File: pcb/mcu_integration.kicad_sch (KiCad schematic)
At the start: 28 parts, among them J1 Micro_SD_Card, U1 STM32F103RBTx, Y1 ECS-80-18-5PX-GM-TR

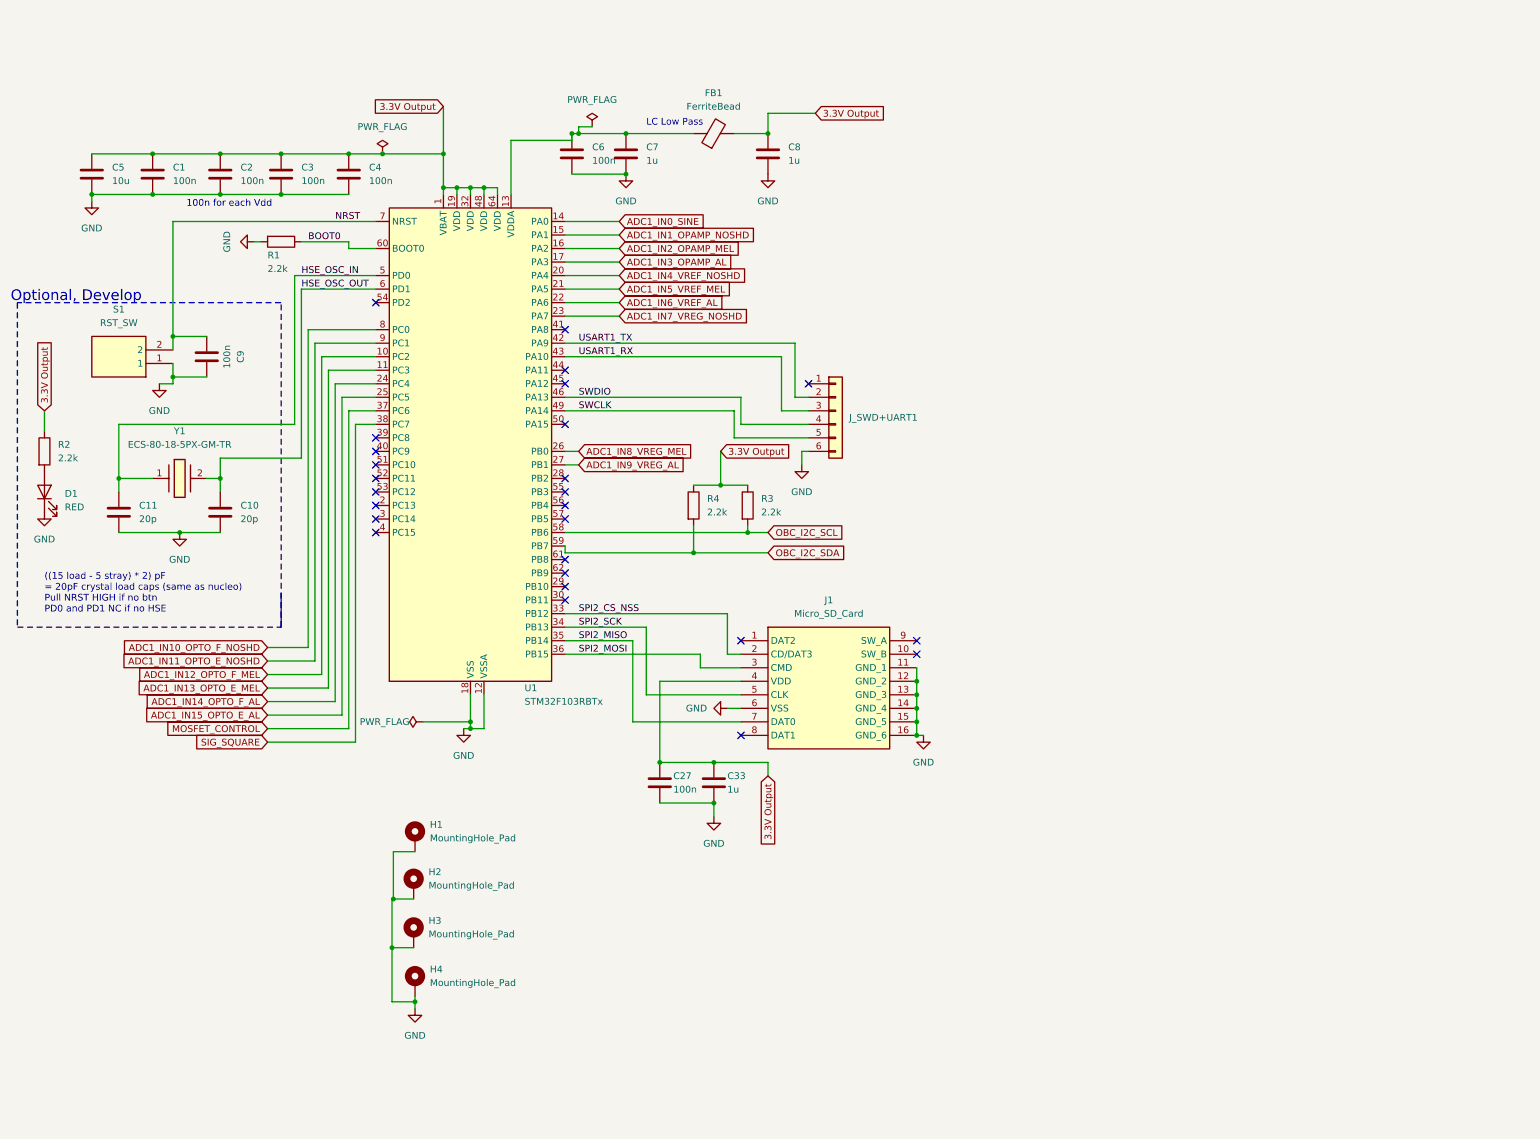
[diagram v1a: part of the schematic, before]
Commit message: SD card change
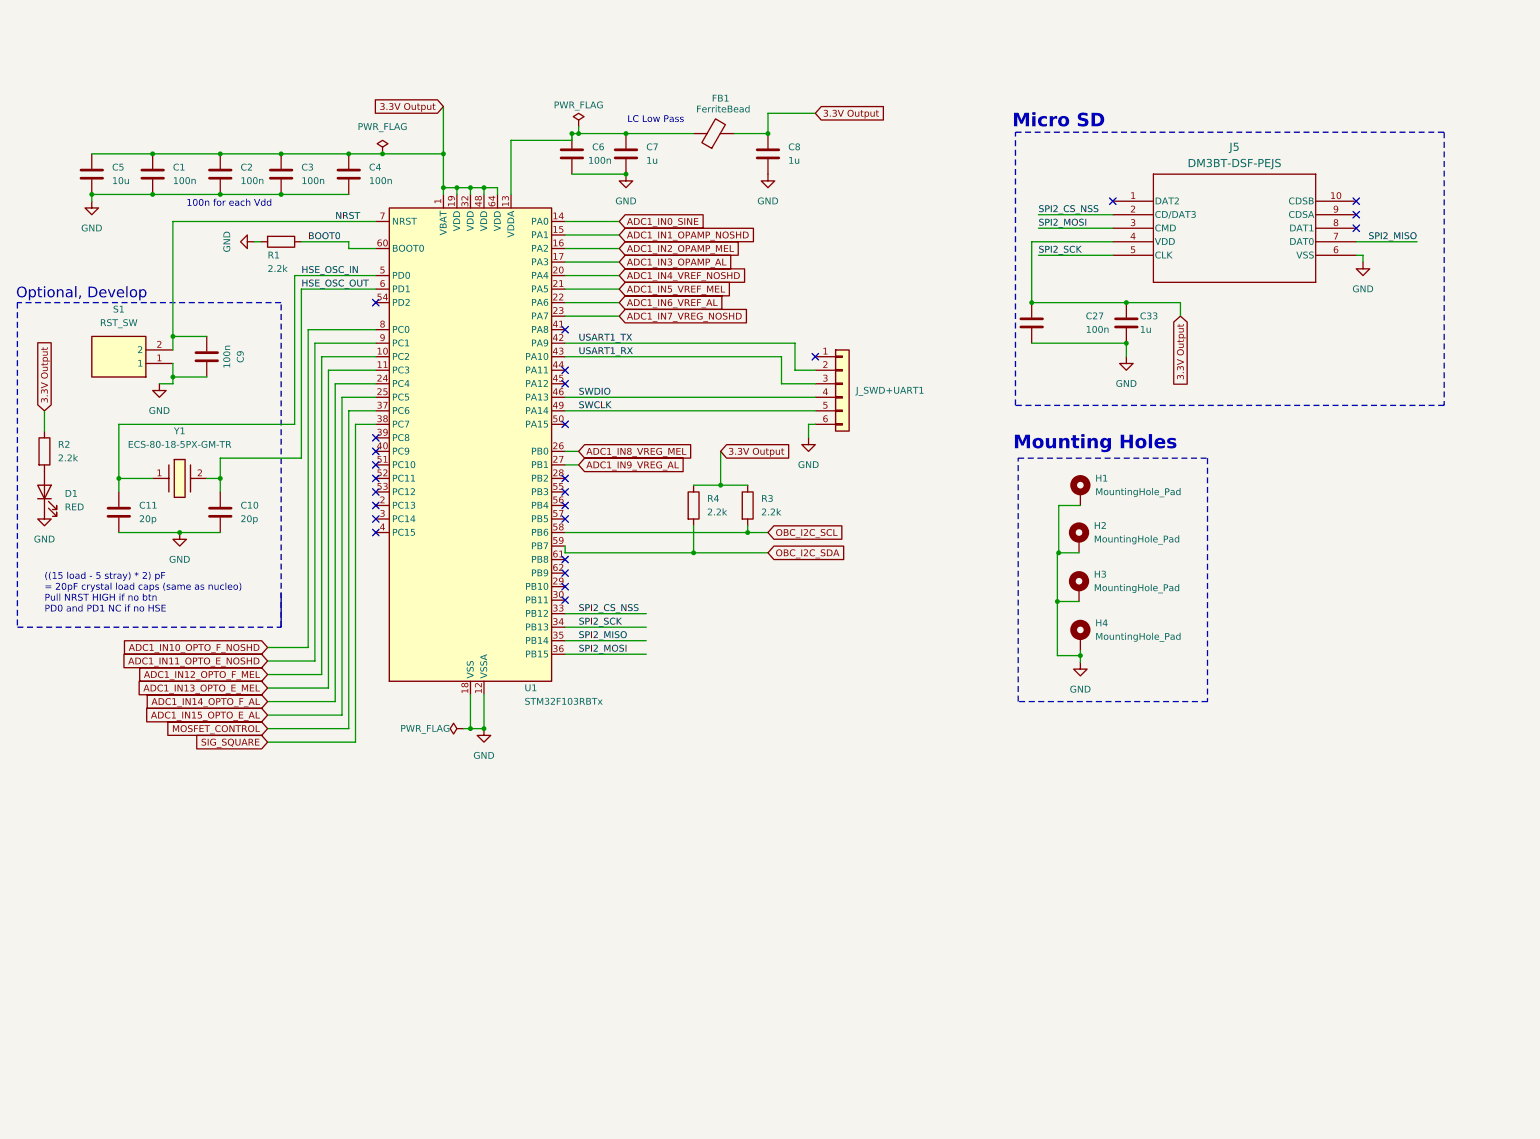
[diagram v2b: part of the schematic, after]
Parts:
- removed J1: Micro_SD_Card, capstone:22017781, symbol capstone:2201778-1
- added J5: DM3BT-DSF-PEJS, capstone:DM3BT_DSF_PEJS, symbol capstone:DM3BT-DSF-PEJS
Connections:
- net 3.3V Output: now also J5.4 (VDD)
- net GND: now also J5.6 (VSS)
- net SPI2_CS_NSS: now also J5.2 (CD/DAT3)
- net SPI2_MISO: now also J5.7 (DAT0)
- net SPI2_MOSI: now also J5.3 (CMD)
- net SPI2_SCK: now also J5.5 (CLK)
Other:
- note added: "Micro SD"
- note added: "Mounting Holes"
- moved on the sheet: C27, C33, H1, H2, H3, H4, J_SWD+UART1

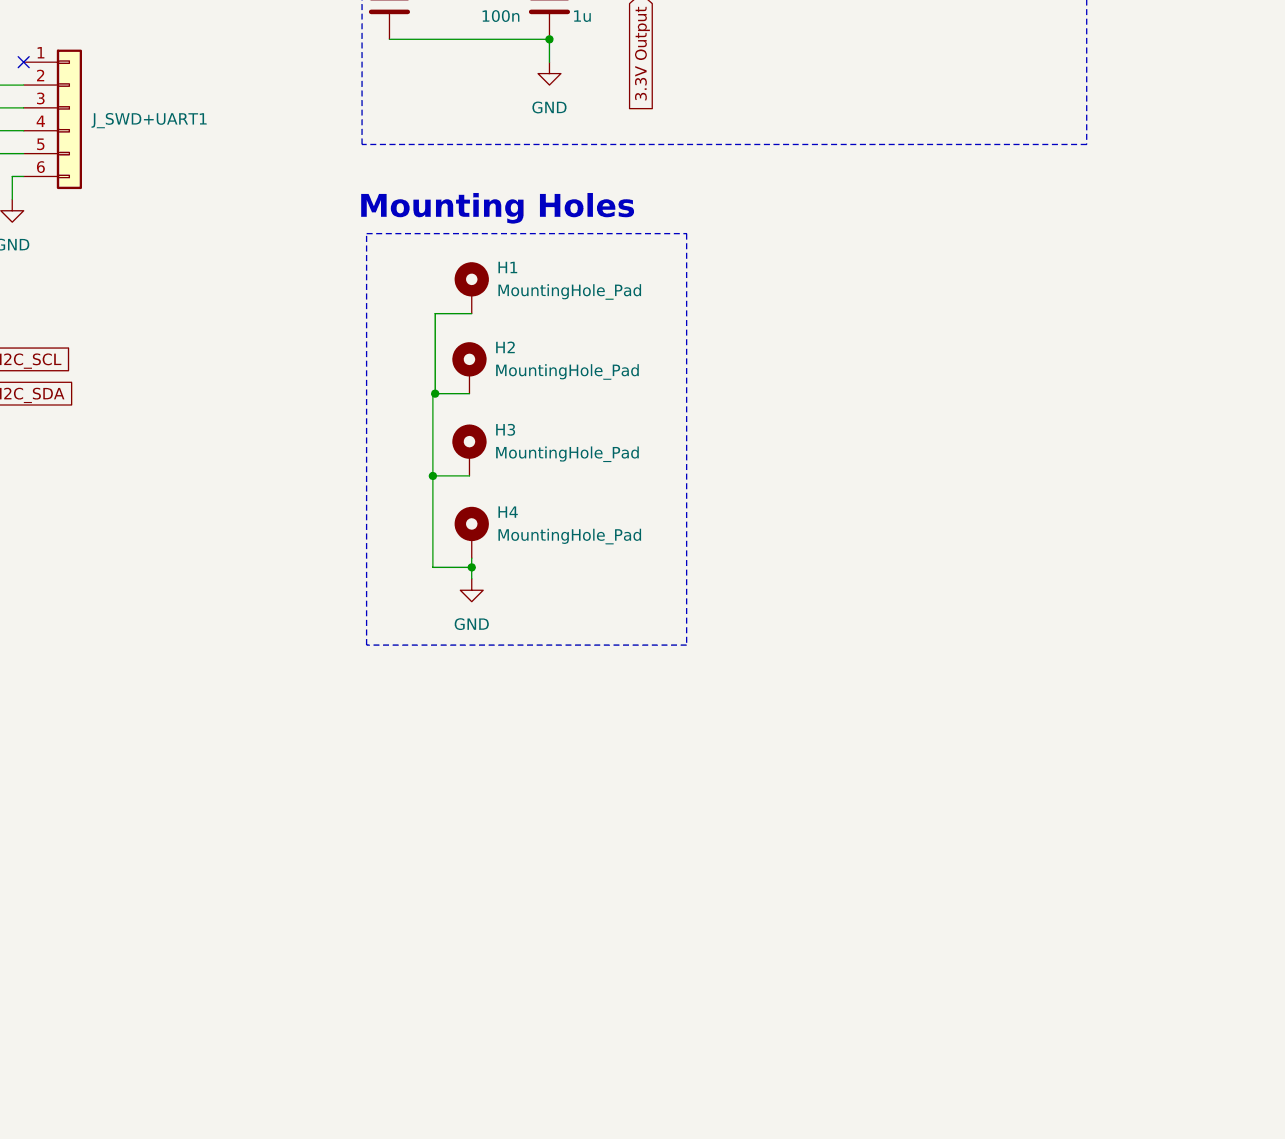
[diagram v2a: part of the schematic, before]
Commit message: Added LM35 Temp Sensor
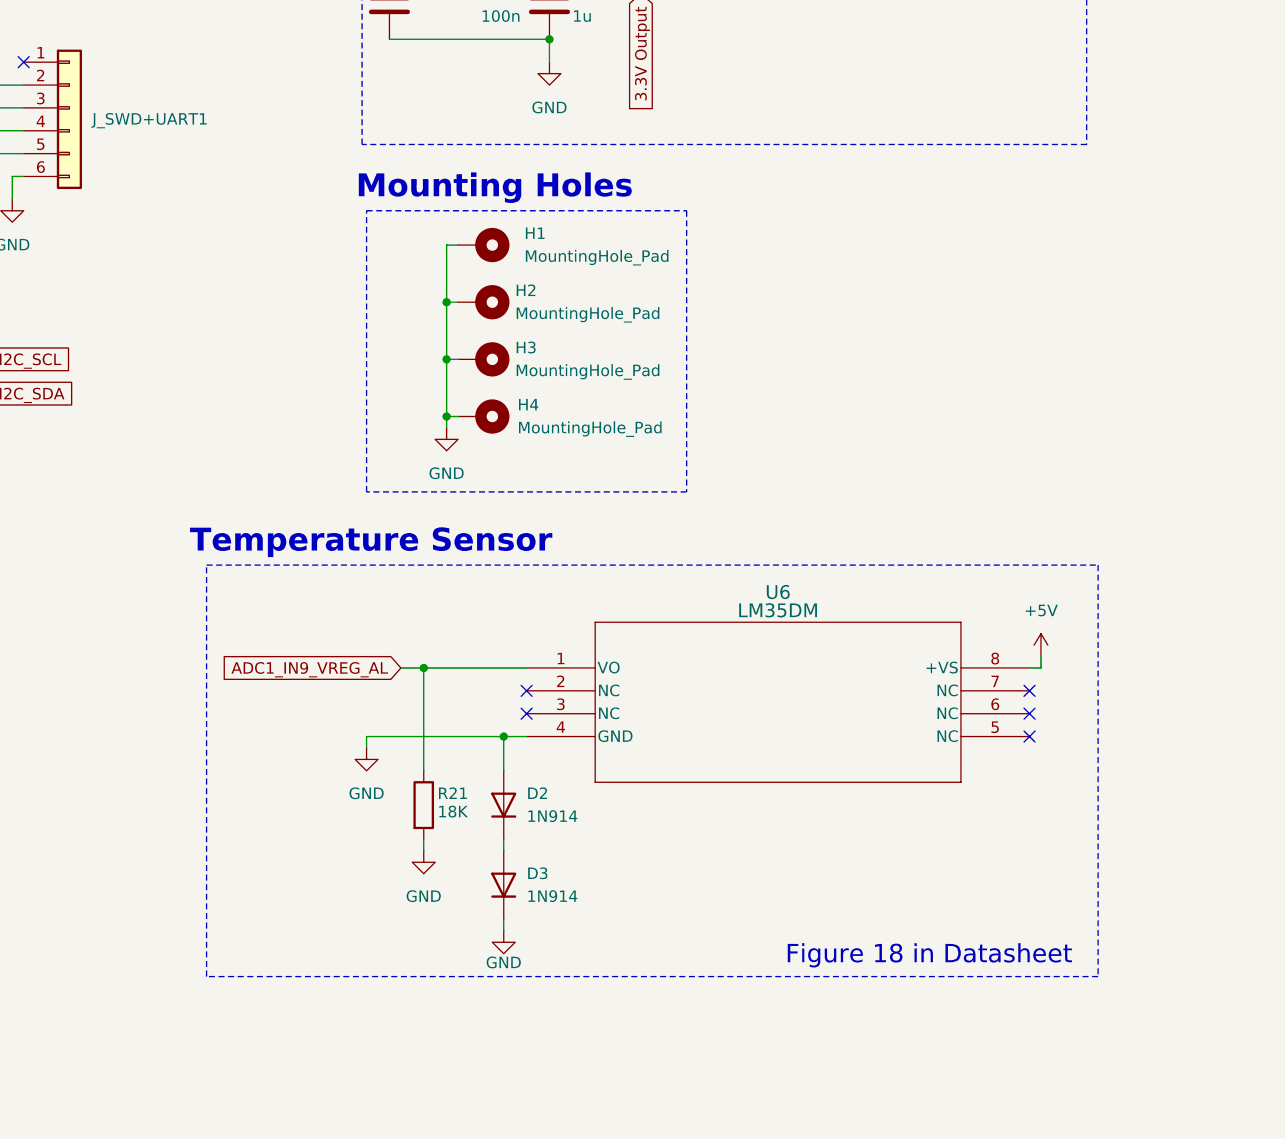
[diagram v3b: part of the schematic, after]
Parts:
- added D2, D3: 1N914, Diode_SMD:D_0402_1005Metric, symbol Device:D
- added R21: 18K, Resistor_SMD:R_0402_1005Metric, symbol Device:R
- added U6: LM35DM, capstone:LM35DM, symbol capstone:LM35DM
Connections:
- net ADC1_IN9_VREG_AL: now also R21.1, U6.1 (VO)
- net GND: now also D2.2 (A), D3.1 (K), R21.2, U6.4 (GND)
- new net: D2.1 (K), D3.2 (A)
- new net +5V: U6.8 (+VS)
- no-connect marks 26 -> 31
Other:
- note added: "Figure 18 in Datasheet"
- note added: "Temperature Sensor"
- moved on the sheet: H1, H2, H3, H4
